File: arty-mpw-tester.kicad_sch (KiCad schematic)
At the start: 115 parts, among them J1 USB4105-GF-A, J10 61300211121, J11 61300211121, J12 61300211121, J14 61300311121, J15 61300311121, J18 61300411121, J19 61300711121, J20 61300411121, J3 arty_chipKIT_connector, J4 61300211121, J5 61300311121, J6 61300211121, J7 61300211121, J8 61300211121, J9 61300211121, Q1 DTC014TEBTL, SW1 JS202011JCQN, SW2 JS202011JCQN, SW3 JS202011JCQN, U1 SN74LVC1G125DCKR, U10 TPD4E02B04DQA, U2 FT232HQ, U3 SN74LVC1G125DCKR, U4 MAX811REUS+T, U5 NTS0102DP, U6 MCP4661-103E/ML, U7 Caravel_breakout_PCB, U8 W25Q32FVSS, U9 MIC2211-AAYML-TR, Y1 ABM8G-12.000MHZ-18-D2Y-T, Y2 ECS-2520MVLC-100-BN-TR

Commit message: Update naming convention
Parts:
- C1, C22, C23, C24, C26, C27, C28, C29, C3, C30, C31, C32, C35, C36: footprint mpw-tester-arty-expansion-footprints:0603-cap -> arty-mpw-tester-footprints:0603-cap; symbol mpw-tester-arty-expansion:C_1u_0603 -> arty-mpw-tester:C_1u_0603
- C10, C11, C13, C14, C15, C16, C18, C19, C20, C21, C25, C33, C34, C37, C4, C5, C7, C8: footprint mpw-tester-arty-expansion-footprints:0603-cap -> arty-mpw-tester-footprints:0603-cap; symbol mpw-tester-arty-expansion:C_100n_0603 -> arty-mpw-tester:C_100n_0603
- C12, C2: footprint mpw-tester-arty-expansion-footprints:0603-cap -> arty-mpw-tester-footprints:0603-cap; symbol mpw-tester-arty-expansion:C_4u7_0603 -> arty-mpw-tester:C_4u7_0603
- C17: footprint mpw-tester-arty-expansion-footprints:0603-cap -> arty-mpw-tester-footprints:0603-cap; symbol mpw-tester-arty-expansion:C_10n_0603 -> arty-mpw-tester:C_10n_0603
- C6, C9: footprint mpw-tester-arty-expansion-footprints:0603-cap -> arty-mpw-tester-footprints:0603-cap; symbol mpw-tester-arty-expansion:C_18p_0603 -> arty-mpw-tester:C_18p_0603
- D1, D2, D3, D4: footprint mpw-tester-arty-expansion-footprints:LED_0603 -> arty-mpw-tester-footprints:LED_0603; symbol mpw-tester-arty-expansion:KP-1608ZGC -> arty-mpw-tester:KP-1608ZGC
- D5, D6, D9: footprint mpw-tester-arty-expansion-footprints:SOD-323F -> arty-mpw-tester-footprints:SOD-323F; symbol mpw-tester-arty-expansion:PMEG6002EJ,115 -> arty-mpw-tester:PMEG6002EJ,115
- D7, D8: footprint mpw-tester-arty-expansion-footprints:SOD-123 -> arty-mpw-tester-footprints:SOD-123; symbol mpw-tester-arty-expansion:1N5819HW-7-F -> arty-mpw-tester:1N5819HW-7-F
- J1: footprint mpw-tester-arty-expansion-footprints:GCT_USB4105-GF-A -> arty-mpw-tester-footprints:GCT_USB4105-GF-A; symbol mpw-tester-arty-expansion:USB4105-GF-A -> arty-mpw-tester:USB4105-GF-A
- J10, J11, J12, J4, J6, J7, J8, J9: footprint mpw-tester-arty-expansion-footprints:PinHeader_1x2_P2.54_Drill0.9mm -> arty-mpw-tester-footprints:PinHeader_1x2_P2.54_Drill0.9mm; symbol mpw-tester-arty-expansion:61300211121 -> arty-mpw-tester:61300211121
- J14, J15, J5: footprint mpw-tester-arty-expansion-footprints:PinHeader_1x3_P2.54_Drill1.1mm -> arty-mpw-tester-footprints:PinHeader_1x3_P2.54_Drill1.1mm; symbol mpw-tester-arty-expansion:61300311121 -> arty-mpw-tester:61300311121
- J18, J20: footprint mpw-tester-arty-expansion-footprints:PinHeader_1x4_P2.54mm_Drill1.02mm -> arty-mpw-tester-footprints:PinHeader_1x4_P2.54mm_Drill1.02mm; symbol mpw-tester-arty-expansion:61300411121 -> arty-mpw-tester:61300411121
- J19: footprint mpw-tester-arty-expansion-footprints:61300711121 -> arty-mpw-tester-footprints:61300711121; symbol mpw-tester-arty-expansion:61300711121 -> arty-mpw-tester:61300711121
- J3: footprint mpw-tester-arty-expansion-footprints:ARTY_A7_SHIELD -> arty-mpw-tester-footprints:ARTY_A7_SHIELD; symbol mpw-tester-arty-expansion:arty_chipKIT_connector -> arty-mpw-tester:arty_chipKIT_connector
- Q1: footprint mpw-tester-arty-expansion-footprints:SOT-416 -> arty-mpw-tester-footprints:SOT-416; symbol mpw-tester-arty-expansion:DTC014TEBTL -> arty-mpw-tester:DTC014TEBTL
- R1, R16, R17, R18, R19, R20, R21, R26, R28, R30, R32, R33, R34, R6: footprint mpw-tester-arty-expansion-footprints:0603-res -> arty-mpw-tester-footprints:0603-res; symbol mpw-tester-arty-expansion:R_10k_0603 -> arty-mpw-tester:R_10k_0603
- R10, R12, R13, R9: footprint mpw-tester-arty-expansion-footprints:0603-res -> arty-mpw-tester-footprints:0603-res; symbol mpw-tester-arty-expansion:R_470R_0603 -> arty-mpw-tester:R_470R_0603
- R11, R14, R15, R29, R35, R8: footprint mpw-tester-arty-expansion-footprints:0603-res -> arty-mpw-tester-footprints:0603-res; symbol mpw-tester-arty-expansion:R_0R_0603 -> arty-mpw-tester:R_0R_0603
- R2, R3: footprint mpw-tester-arty-expansion-footprints:0603-res -> arty-mpw-tester-footprints:0603-res; symbol mpw-tester-arty-expansion:R_5k1_0603 -> arty-mpw-tester:R_5k1_0603
- R22: footprint mpw-tester-arty-expansion-footprints:0603-res -> arty-mpw-tester-footprints:0603-res; symbol mpw-tester-arty-expansion:R_68k_0603 -> arty-mpw-tester:R_68k_0603
- R23: footprint mpw-tester-arty-expansion-footprints:0603-res -> arty-mpw-tester-footprints:0603-res; symbol mpw-tester-arty-expansion:R_41k2_0603 -> arty-mpw-tester:R_41k2_0603
- R24: footprint mpw-tester-arty-expansion-footprints:0603-res -> arty-mpw-tester-footprints:0603-res; symbol mpw-tester-arty-expansion:R_15k_0603 -> arty-mpw-tester:R_15k_0603
- R25: footprint mpw-tester-arty-expansion-footprints:0603-res -> arty-mpw-tester-footprints:0603-res; symbol mpw-tester-arty-expansion:R_34k_0603 -> arty-mpw-tester:R_34k_0603
- R27, R31: footprint mpw-tester-arty-expansion-footprints:0603-res -> arty-mpw-tester-footprints:0603-res; symbol mpw-tester-arty-expansion:R_4k7_0603 -> arty-mpw-tester:R_4k7_0603
- R4, R5: footprint mpw-tester-arty-expansion-footprints:0402-res -> arty-mpw-tester-footprints:0402-res; symbol mpw-tester-arty-expansion:R_0R_0402 -> arty-mpw-tester:R_0R_0402
- R7: footprint mpw-tester-arty-expansion-footprints:0603-res -> arty-mpw-tester-footprints:0603-res; symbol mpw-tester-arty-expansion:R_12k_1%_0603 -> arty-mpw-tester:R_12k_1%_0603
- S1: footprint mpw-tester-arty-expansion-footprints:SW_SPST_4.2x2.8 -> arty-mpw-tester-footprints:SW_SPST_4.2x2.8; symbol mpw-tester-arty-expansion:KMR2 -> arty-mpw-tester:KMR2
- SW1, SW2, SW3: footprint mpw-tester-arty-expansion-footprints:JS202011JCQN -> arty-mpw-tester-footprints:JS202011JCQN; symbol mpw-tester-arty-expansion:JS202011JCQN -> arty-mpw-tester:JS202011JCQN
- TP1: footprint mpw-tester-arty-expansion-footprints:PROBE_PAD_1206 -> arty-mpw-tester-footprints:PROBE_PAD_1206; symbol mpw-tester-arty-expansion:RCW-0C -> arty-mpw-tester:RCW-0C
- U1, U3: footprint mpw-tester-arty-expansion-footprints:SOT-353 -> arty-mpw-tester-footprints:SOT-353; symbol mpw-tester-arty-expansion:SN74LVC1G125DCKR -> arty-mpw-tester:SN74LVC1G125DCKR
- U10: footprint mpw-tester-arty-expansion-footprints:USON-10_2.5x1.0mm_P0.5mm -> arty-mpw-tester-footprints:USON-10_2.5x1.0mm_P0.5mm; symbol mpw-tester-arty-expansion:TPD4E02B04DQA -> arty-mpw-tester:TPD4E02B04DQA
- U2: footprint mpw-tester-arty-expansion-footprints:QFN-48-1EP_8x8mm_P0.5mm_EP6.2x6.2mm_FT232HQ_marking -> arty-mpw-tester-footprints:QFN-48-1EP_8x8mm_P0.5mm_EP6.2x6.2mm_FT232HQ_marking; symbol mpw-tester-arty-expansion:FT232HQ -> arty-mpw-tester:FT232HQ
- U4: footprint mpw-tester-arty-expansion-footprints:SOT-143-4 -> arty-mpw-tester-footprints:SOT-143-4; symbol mpw-tester-arty-expansion:MAX811REUS+T -> arty-mpw-tester:MAX811REUS+T
- U5: footprint mpw-tester-arty-expansion-footprints:TSSOP-8_W3mm -> arty-mpw-tester-footprints:TSSOP-8_W3mm; symbol mpw-tester-arty-expansion:NTS0102DP -> arty-mpw-tester:NTS0102DP
- U6: footprint mpw-tester-arty-expansion-footprints:QFN-16_EP_4x4_Pitch0.65mm -> arty-mpw-tester-footprints:QFN-16_EP_4x4_Pitch0.65mm; symbol mpw-tester-arty-expansion:MCP4661-103E/ML -> arty-mpw-tester:MCP4661-103E/ML
- U7: footprint mpw-tester-arty-expansion-footprints:caravel_breakout -> arty-mpw-tester-footprints:caravel_breakout; symbol mpw-tester-arty-expansion:Caravel_breakout_PCB -> arty-mpw-tester:Caravel_breakout_PCB
- U8: footprint mpw-tester-arty-expansion-footprints:SOIC127P790X216-8N -> arty-mpw-tester-footprints:SOIC127P790X216-8N; symbol mpw-tester-arty-expansion:W25Q32FVSS -> arty-mpw-tester:W25Q32FVSS
- U9: footprint mpw-tester-arty-expansion-footprints:DFN-10-1EP_3x3mm -> arty-mpw-tester-footprints:DFN-10-1EP_3x3mm; symbol mpw-tester-arty-expansion:MIC2211-AAYML-TR -> arty-mpw-tester:MIC2211-AAYML-TR
- Y1: footprint mpw-tester-arty-expansion-footprints:KX-7 -> arty-mpw-tester-footprints:KX-7; symbol mpw-tester-arty-expansion:ABM8G-12.000MHZ-18-D2Y-T -> arty-mpw-tester:ABM8G-12.000MHZ-18-D2Y-T
- Y2: footprint mpw-tester-arty-expansion-footprints:Oscillator_SMD_ECS_2520MV-xxx-xx-4Pin_2.5x2.0mm -> arty-mpw-tester-footprints:Oscillator_SMD_ECS_2520MV-xxx-xx-4Pin_2.5x2.0mm; symbol mpw-tester-arty-expansion:ECS-2520MVLC-100-BN-TR -> arty-mpw-tester:ECS-2520MVLC-100-BN-TR
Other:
- title: MPW tester Arty expansion -> Arty MPW Tester

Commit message: Update caravel-breakout footprint with more detailed 3D model and flexypins
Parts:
- removed U7: Caravel_breakout_PCB, arty-mpw-tester-footprints:caravel_breakout, symbol arty-mpw-tester:Caravel_breakout_PCB
- added U7: Caravel_breakout_PCB_flexypin, arty-mpw-tester-footprints:caravel-breakout-flexypin, symbol arty-mpw-tester:Caravel_breakout_PCB_flexypin
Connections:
- net ADBUS0: now also U7.38 (SCK_IO4)
- net ADBUS1: now also U7.40 (SDI_IO2)
- net ADBUS2: now also U7.41 (SDO_IO1)
- net ADBUS3: now also U7.39 (~{CS}_IO3)
- net AGND: now also U7.5 (GND), U7.8 (GND); no longer J3.26 (GND)
- net ARTY_MEM_CS: no longer J3.25 (SS)
- net ARTY_MEM_MISO: no longer J3.28 (MISO)
- net ARTY_MEM_MOSI: no longer J3.29 (MOSI)
- net ARTY_MEM_SCK: no longer J3.27 (SCK)
- net CRVL_GPIO: now also U7.47 (GPIO)
- net CRVL_IO0: now also U7.42 (IO0)
- net CRVL_IO10: now also U7.32 (IO10)
- net CRVL_IO11: now also U7.31 (IO11)
- net CRVL_IO12: now also U7.30 (IO12)
- net CRVL_IO13: now also U7.29 (IO13)
- net CRVL_IO14: now also U7.28 (IO14)
- net CRVL_IO15: now also U7.27 (IO15)
- net CRVL_IO16: now also U7.26 (IO16)
- net CRVL_IO17: now also U7.25 (IO17)
- net CRVL_IO18: now also U7.24 (IO18)
- net CRVL_IO19: now also U7.23 (IO19)
- net CRVL_IO20: now also U7.22 (IO20)
- net CRVL_IO21: now also U7.21 (IO21)
- net CRVL_IO22: now also U7.20 (IO22)
- net CRVL_IO23: now also U7.19 (IO23)
- net CRVL_IO24: now also U7.18 (IO24)
- net CRVL_IO25: now also U7.17 (IO25)
- net CRVL_IO26: now also U7.16 (IO26)
- net CRVL_IO27: now also U7.15 (IO27)
- net CRVL_IO28: now also U7.14 (IO28)
- net CRVL_IO29: now also U7.13 (IO29)
- net CRVL_IO30: now also U7.12 (IO30)
- net CRVL_IO31: now also U7.11 (IO31)
- net CRVL_IO32: now also U7.10 (IO32)
- net CRVL_IO33: now also U7.9 (IO33)
- net CRVL_IO34: now also U7.4 (IO34)
- net CRVL_IO35: now also U7.3 (IO35)
- net CRVL_IO36: now also U7.2 (IO36)
- net CRVL_IO37: now also U7.1 (IO37)
- net CRVL_IO5: now also U7.37 (RX_IO5)
- net CRVL_IO6: now also U7.36 (TX_IO6)
- net CRVL_IO7: now also U7.35 (IO7)
- net CRVL_IO8: now also U7.34 (IO8)
- net CRVL_IO9: now also U7.33 (IO9)
- net CRVL_XCLK: now also U7.52 (XCLK)
- net CRVL_~{RST}: now also U7.53 (~{RST})
- net MEM.SCK: now also U7.46 (FLASH_SCK)
- net MEM.SI: now also U7.49 (FLASH_D0)
- net MEM.SO: now also U7.48 (FLASH_D1)
- net MEM.~{CS}: now also U7.51 (~{FLASH_CS})
- net VCCD: now also U7.50 (VCCD), U7.6 (VCCD)
- net VCCD1: now also U7.43 (VCCD1)
- net VCCD2: now also U7.56 (VCCD2)
- net VDDA: now also U7.45 (VDDA)
- net VDDA1: now also U7.44 (VDDA1)
- net VDDA2: now also U7.54 (VDDA2)
- net VDDIO: now also U7.55 (VDDIO), U7.7 (VDDIO)

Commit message: Rotate slide switches so 3D models match default configuration. Update Arty A7 shield connector side
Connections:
- net AGND: now also J3.26 (GND), SW2.6 (2_C); no longer SW2.2 (1_C)
- net ARTY_MEM_CS: now also J3.25 (SS)
- net ARTY_MEM_MISO: now also J3.28 (MISO)
- net ARTY_MEM_MOSI: now also J3.29 (MOSI)
- net ARTY_MEM_SCK: now also J3.27 (SCK)
- net VBUS: now also SW3.3, SW3.7; no longer SW3.1, SW3.5
- net ~{UART_EN}: now also SW2.7; no longer SW2.1
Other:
- moved on the sheet: SW3

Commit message: Exchanged FT232 to FT4232 on schematics
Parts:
- removed C10, C13, C4, C5, C7, C8: C_100n_0603, arty-mpw-tester-footprints:0603-cap, symbol arty-mpw-tester:C_100n_0603
- removed C12, C2: C_4u7_0603, arty-mpw-tester-footprints:0603-cap, symbol arty-mpw-tester:C_4u7_0603
- removed D1, D2: KP-1608ZGC, arty-mpw-tester-footprints:LED_0603, symbol arty-mpw-tester:KP-1608ZGC
- removed D5: PMEG6002EJ,115, arty-mpw-tester-footprints:SOD-323F, symbol arty-mpw-tester:PMEG6002EJ,115
- removed R1: R_10k_0603, arty-mpw-tester-footprints:0603-res, symbol arty-mpw-tester:R_10k_0603
- removed R10, R9: R_470R_0603, arty-mpw-tester-footprints:0603-res, symbol arty-mpw-tester:R_470R_0603
- removed SW2: JS202011JCQN, arty-mpw-tester-footprints:JS202011JCQN, symbol arty-mpw-tester:JS202011JCQN
- removed U1, U3: SN74LVC1G125DCKR, arty-mpw-tester-footprints:SOT-353, symbol arty-mpw-tester:SN74LVC1G125DCKR
- removed U2: FT232HQ, arty-mpw-tester-footprints:QFN-48-1EP_8x8mm_P0.5mm_EP6.2x6.2mm_FT232HQ_marking, symbol arty-mpw-tester:FT232HQ
- added C10, C13, C5, C7: C_4u7_0603, arty-mpw-tester-footprints:0603-cap, symbol arty-mpw-tester:C_4u7_0603
- added C12, C38: C_100n_0603, arty-mpw-tester-footprints:0603-cap, symbol arty-mpw-tester:C_100n_0603
- added C2: C_1u_0603, arty-mpw-tester-footprints:0603-cap, symbol arty-mpw-tester:C_1u_0603
- added C4: C_10n_0603, arty-mpw-tester-footprints:0603-cap, symbol arty-mpw-tester:C_10n_0603
- added C8: C_10u_0603, antmicro-footprints:0603-cap, symbol antmicroCapacitors0603:C_10u_0603
- added FB1, FB2, FB3: BLM18SG121TN1D, antmicro-footprints:0603-res, symbol antmicroFerriteBeadsandChips:BLM18SG121TN1D
- added U1: TAR5S33UTE85LF, antmicro-footprints:SOT-353, symbol antmicroPMICVoltageRegulatorsLinear:TAR5S33UTE85LF
- added U2: FT4232H-56Q, antmicro-footprints:QFN-56-1EP_8x8mm_P0.5mm_EP5.5.9x5.9mm, symbol antmicroInterfaceControllers:FT4232H-56Q
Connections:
- net VCCA is gone; now on net VCORE: C14.1
- net ADBUS0: now also U2.32 (CDBUS0); no longer J3.35 (IO37), U7.38 (SCK_IO4)
- net ADBUS1: now also U2.33 (CDBUS1); no longer J3.34 (IO38), U7.40 (SDI_IO2)
- net FTDI_DN: now also U2.7 (DM)
- net FTDI_DP: now also U2.8 (DP)
- net FTDI_EN_VOUT1: now also U2.27 (BDBUS5)
- net FTDI_EN_VOUT2: now also U2.28 (BDBUS6)
- net FTDI_~{MR}: now also U2.26 (BDBUS4)
- net MEM.SCK: now also U2.22 (BDBUS0)
- net MEM.SI: now also U2.24 (BDBUS2)
- net MEM.SO: now also U2.23 (BDBUS1)
- net MEM.~{CS}: now also U2.25 (BDBUS3)
- net REF: now also U2.6 (REF)
- net VBUS: now also C2.1, U1.1 (EN), U1.5 (VIN)
- net VCORE: now also C13.1, U2.2 (VCORE), U2.31 (VCORE), U2.43 (VREGOUT)
- net XIN: now also U2.3 (OSCI)
- net XOUT: now also U2.4 (OSCO)
- net ADBUS2 renamed CRVL_IO1
- net CRVL_IO1: now also U2.14 (ADBUS2)
- net ADBUS3 renamed CRVL_IO3
- net CRVL_IO3: now also U2.15 (ADBUS3)
- net AGND renamed EP
- net EP: now also C10.2, C12.2, C13.2, C2.2, C38.2, C4.2, C5.2, C7.2, C8.2, U1.2 (GND), U2.10 (TEST), U2.21 (GND), U2.41 (GND), U2.45 (GND), U2.57 (GND)
- net FTDI_3V3 renamed 3V3_FTDI
- net 3V3_FTDI: now also C12.1, C38.1, FB1.1, FB2.1, FB3.2, U2.16 (VCCIO), U2.36 (VCCIO), U2.44 (VREGIN), U2.50 (VCCIO); no longer C16.1
- net FTDI_RESET renamed FTDI_RST
- net FTDI_RST: now also U2.11 (RESET)
- new net: C4.1, U1.3 (Noise)
- new net: C8.1, FB3.1, U1.4 (VOUT)
- new net CRVL_IO2: J3.34 (IO38), U2.13 (ADBUS1), U7.40 (SDI_IO2)
- new net CRVL_IO4: J3.35 (IO37), U2.12 (ADBUS0), U7.38 (SCK_IO4)
- new net VPHY: C10.1, C5.1, FB1.2, U2.5 (VPHY)
- new net VPLL: C16.1, C7.1, FB2.2, U2.9 (VPLL)
- no-connect marks 29 -> 37
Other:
- note added: "CS1_1"
- note added: "CS1_2"
- note added: "MISO_1"
- note added: "MISO_2"
- note added: "MOSI_1"
- note added: "MOSI_2"
- note added: "RXD"
- note added: "SCK_1"
- note added: "SCK_2"
- note added: "TXD"
- note removed: "Buffer ENABLE"
- note removed: "LDO OUT"
- note removed: "MISO / RXD"
- note removed: "SCK / TXD"
- note removed: "Serial buffer"
- moved on the sheet: C1, C11, C16, C17, C19, C20, C22, C23, C24, C26, C27, C28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

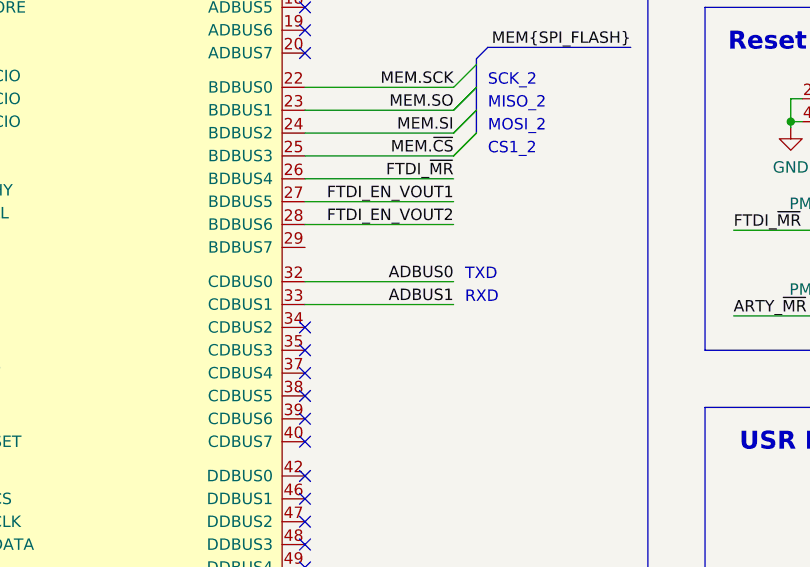
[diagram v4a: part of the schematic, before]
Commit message: Renamed FTDI UART to Caravel net after buffers removal
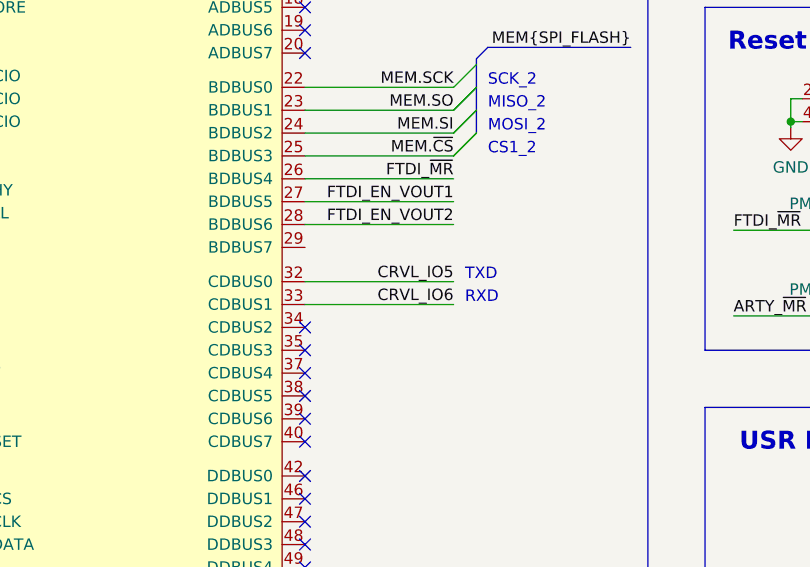
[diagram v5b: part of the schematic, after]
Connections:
- net ADBUS0 is gone; now on net CRVL_IO5: U2.32 (CDBUS0)
- net ADBUS1 is gone; now on net CRVL_IO6: U2.33 (CDBUS1)
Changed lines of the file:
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@@
     (effects (font (size 1.27 1.27)) (justify left bottom))
+  )
+  (label "CRVL_IO5" (at 154.94 88.9 180)
+    (effects (font (size 1.27 1.27)) (justify right bottom))
   )
   (label "CRVL_IO10" (at 140.335 208.28 0)
@@
     (effects (font (size 1.27 1.27)) (justify right bottom))
   )
+  (label "CRVL_IO6" (at 154.94 91.44 180)
+    (effects (font (size 1.27 1.27)) (justify right bottom))
+  )
   (label "CRVL_IO13" (at 396.875 179.07 180)
     (effects (font (size 1.27 1.27)) (justify right bottom))
@@
     (effects (font (size 1.27 1.27)) (justify left bottom))
   )
-  (label "ADBUS1" (at 154.94 91.44 180)
-    (effects (font (size 1.27 1.27)) (justify right bottom))
-  )
   (label "CRVL_IO7" (at 140.335 200.66 0)
     (effects (font (size 1.27 1.27)) (justify left bottom))
@@
     (effects (font (size 1.27 1.27)) (justify left bottom))
   )
-  (label "ADBUS0" (at 154.94 88.9 180)
-    (effects (font (size 1.27 1.27)) (justify right bottom))
-  )
   (label "CRVL_XCLK" (at 236.855 220.98 0)
